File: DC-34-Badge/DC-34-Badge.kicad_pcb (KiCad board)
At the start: 2 copper layers, 104.1 x 123.2 mm, 79 parts, among them J2 62684-402100ALF, J3 Conn_02x03_Odd_Even, J4 Conn_02x03_Odd_Even, J5 Conn_02x03_Odd_Even, J6 Motor_Attachment, Q1 2SC1815, SW1 SW_Push_DPDT, SW10 SW_DIP_x02, SW11 SW_DIP_x02, SW2 SW_DIP_x02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

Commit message: Updated circuit.
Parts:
- added J1: 2171790001, 2171790001:MOLEX_2171790001, F.Cu at (132.1, 38.1)
- U1: value ESP32-S3-MINI-1 -> ESP32-S3-MINI-1-N8; footprint Espressif:ESP32-S3-MINI-1U -> expressif-digikey:XCVR_ESP32-S3-MINI-1-N8
- moved D1 51.8 mm to (114.3, 50.8)
- moved U1 44.4 mm to (101.6, 48.3)
- moved R10 28.6 mm to (96.7, 64.1)
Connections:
- net +BATT renamed BATT
- BZ1 pad 1: +3.3V -> Net-(BZ1-Pad1)
- BZ1 pad 2: Net-(BZ1-Pad2) -> +3.3V
- Q1 pad 2: Net-(BZ1-Pad2) -> Net-(BZ1-Pad1)
- R10 pad 1: Net-(D1-Pad2) -> Net-(R10-Pad1)
- R10 pad 2: Net-(R10-Pad2) -> Net-(D1-Pad2)
- R30 pad 1: Net-(BZ1-Pad2) -> Net-(BZ1-Pad1)
- R31 pad 1: +3.3V -> PHOTO_RES
- R31 pad 2: PHOTO -> +3.3V
- R7 pad 2: PHOTO -> PHOTO_RES
- U1 pad 17: Net-(R10-Pad2) -> Net-(R10-Pad1)
- U1 pad 22: PHOTO -> PHOTO_RES
- U1 pad 23: D- -> D+
- U1 pad 24: D+ -> D-
- U1 pad 29: CS -> unconnected-(U1-Pad29)
- U1 pad 30: GND -> unconnected-(U1-Pad30)
- U1 pad 34: unconnected-(U1-Pad34) -> CS

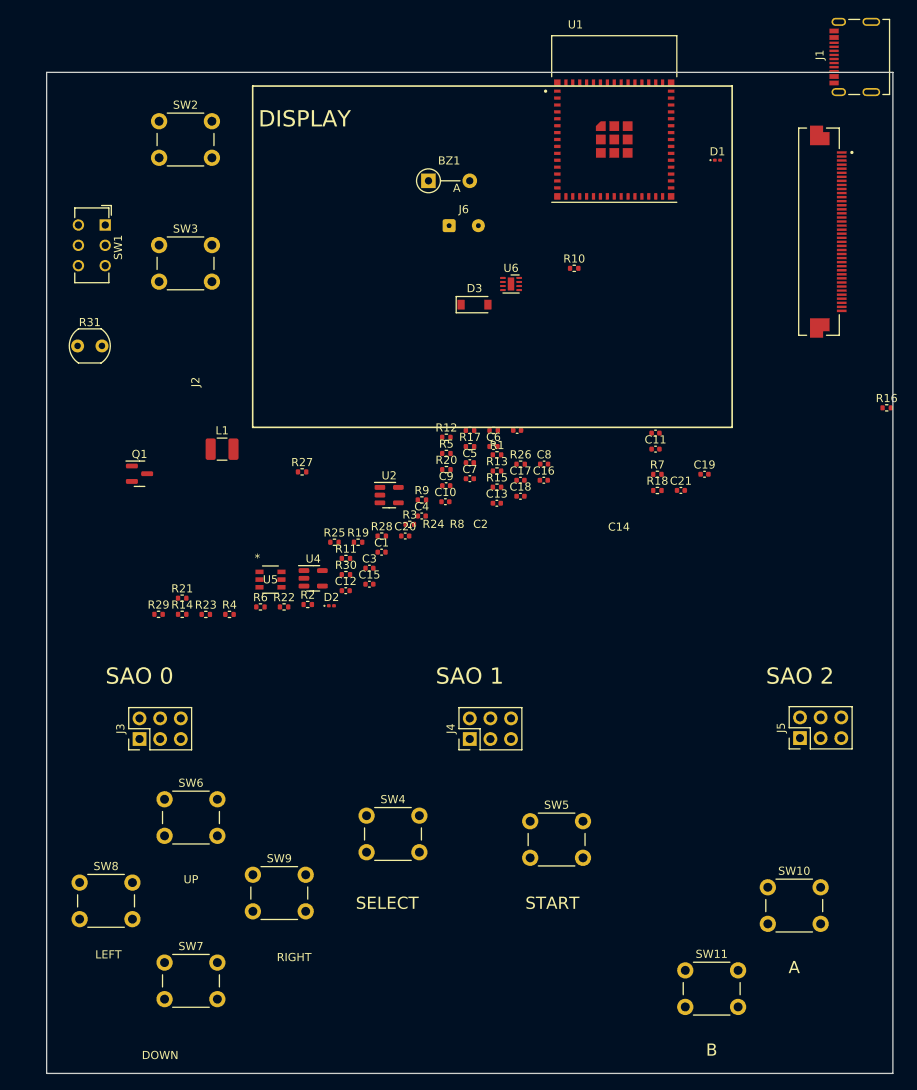
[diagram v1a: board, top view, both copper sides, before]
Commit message: Added footprint libraries and placed componets.
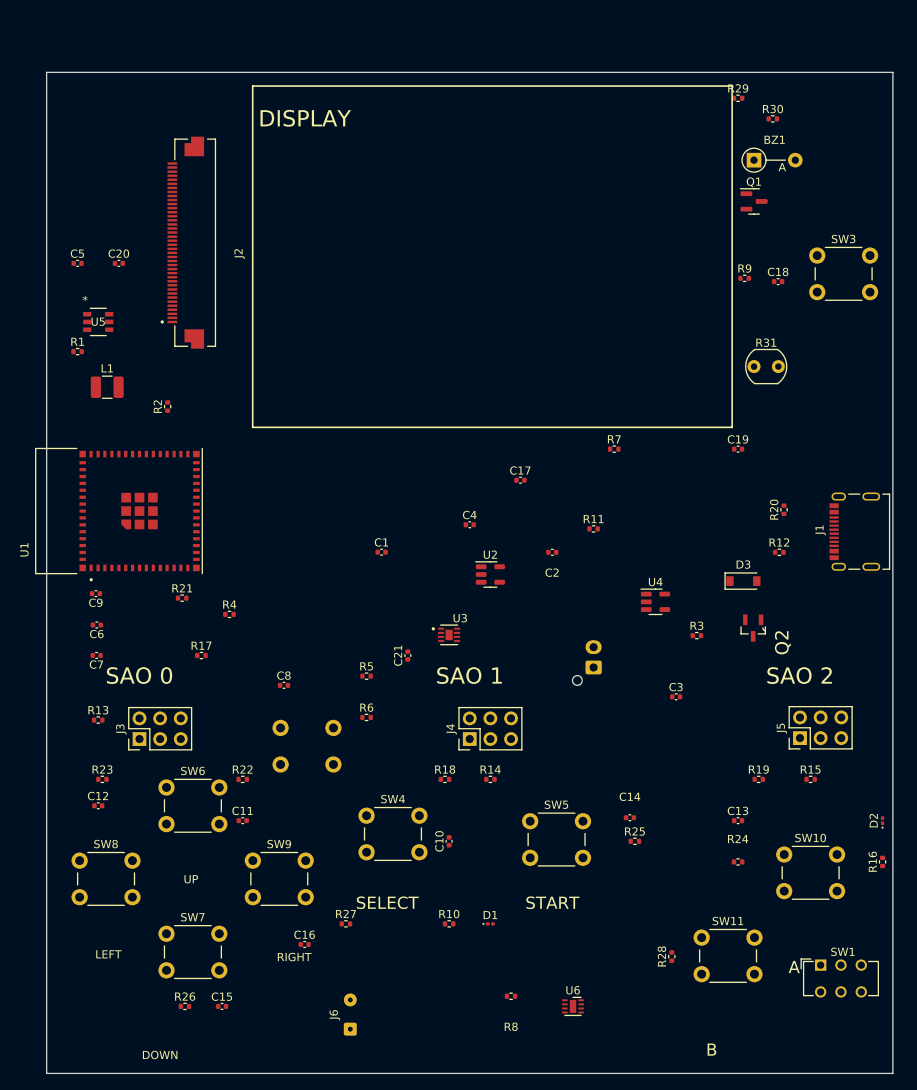
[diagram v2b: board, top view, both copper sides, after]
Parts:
- added J7: Conn_01x02_Male, Connector_JST:JST_XH_B2B-XH-AM_1x02_P2.50mm_Vertical, B.Cu at (99.1, 113.2)
- added Q2: DMG3415U-7, DMG3415U_7:SOT95P240X105-3N, F.Cu at (118.7, 108.4)
- added U3: MAX17048G_T10, MAX17048G:SON50P200X200X80-9N, F.Cu at (81.3, 109.2)
- SW2: moved to B.Cu
- moved SW1 126.7 mm to (127.0, 149.9), turned to 0 degrees
- moved J6 99.6 mm to (69.1, 157.7), turned to 90 degrees
- moved D1 98.0 mm to (86.4, 144.8)
- moved R29 95.5 mm to (116.8, 43.2)
- moved U6 89.2 mm to (96.5, 154.9)
- moved R31 83.3 mm to (118.8, 76.2)
- moved Q1 82.7 mm to (118.8, 55.9)
- moved R10 82.1 mm to (81.3, 144.8)
- moved SW3 81.0 mm to (126.6, 62.5)
- moved R26 78.5 mm to (48.8, 154.9)
- moved SW2 77.7 mm to (67.0, 120.7), turned to 180 degrees
- moved R30 76.8 mm to (121.1, 45.7)
- moved J2 75.2 mm to (50.8, 61.0), turned to 90 degrees
- moved U1 74.2 mm to (43.2, 94.0), turned to 90 degrees
- moved D2 72.8 mm to (134.6, 132.1), turned to 90 degrees
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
